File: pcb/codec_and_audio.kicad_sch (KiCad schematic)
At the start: 15 parts, among them IC3 PCM3060PWR, J3 AudioJack3_Dual_Switch, U1 ${SIM.PARAMS}

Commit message: progress on shcematics
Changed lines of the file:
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@@
     )
   )
-  (hierarchical_label "ENC_LRCK" (shape bidirectional) (at 125.095 97.79 180) (fields_autoplaced)
+  (hierarchical_label "ENC_LRCK" (shape input) (at 125.095 97.79 180) (fields_autoplaced)
     (effects (font (size 1.27 1.27)) (justify right))
   )
@@
     (effects (font (size 1.27 1.27)) (justify right))
   )
-  (hierarchical_label "DEC_LRCK" (shape bidirectional) (at 128.905 130.175 180) (fields_autoplaced)
+  (hierarchical_label "DEC_LRCK" (shape input) (at 128.905 130.175 180) (fields_autoplaced)
     (effects (font (size 1.27 1.27)) (justify right))
   )
@@
     (effects (font (size 1.27 1.27)) (justify right))
   )
-  (hierarchical_label "ENC_BCK" (shape bidirectional) (at 125.095 99.695 180) (fields_autoplaced)
+  (hierarchical_label "ENC_BCK" (shape input) (at 125.095 99.695 180) (fields_autoplaced)
     (effects (font (size 1.27 1.27)) (justify right))
   )
@@
     (effects (font (size 1.27 1.27)) (justify right))
   )
-  (hierarchical_label "DEC_BCK" (shape bidirectional) (at 128.905 128.27 180) (fields_autoplaced)
+  (hierarchical_label "DEC_BCK" (shape input) (at 128.905 128.27 180) (fields_autoplaced)
     (effects (font (size 1.27 1.27)) (justify right))
   )

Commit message: update
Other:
- moved on the sheet: C17, C18, J3A, R1, R2, U1

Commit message: i forgot this
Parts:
- removed C18: 330pF, symbol Device:C
- removed J3: AudioJack3_Dual_Switch, symbol Connector_Audio:AudioJack3_Dual_Switch
- removed R1: R, symbol Device:R
- removed R2: 20k, symbol Device:R
- removed U1: ${SIM.PARAMS}, symbol Simulation_SPICE:OPAMP
- added J3, J4: XLR3_AudioJack2_Combo_Ground, symbol Connector_Audio:XLR3_AudioJack2_Combo_Ground
- C17: value 10uF -> 4u7
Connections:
- net GND: now also J3.1, J3.G, J4.1, J4.G
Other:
- note added: "cold"
- note added: "hot"
- note removed: "high pass filter"
- note removed: "low pass filter"
- note removed: "sleeve is connected to VCOM"
- moved on the sheet: C10, C11, C12, C13, C14, C15, C16, C17, C9, IC3

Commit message: aaaaaa
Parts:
- removed C10, C11: 4.7uF, symbol Device:C_Polarized
- removed C12, C16, C9: 10uF, symbol Device:C_Polarized
- removed IC3: PCM3060PWR, SOP65P640X120-28N, symbol SamacSys_Parts:PCM3060PWR
- removed J4: XLR3_AudioJack2_Combo_Ground, symbol Connector_Audio:XLR3_AudioJack2_Combo_Ground
- added C10, C11, C18: 100nF, symbol Device:C
- added C12, C25, C9: 1uF, symbol Device:C
- added C16: 47uF, symbol Device:C
- added C33: 10uF, symbol Device:C_Polarized
- added C35: 1uF, symbol Device:C_Polarized
- added J4: AudioJack2, symbol Connector_Audio:AudioJack2
- added J5: XLR3_Ground, symbol Connector_Audio:XLR3_Ground
- added R2, R6: 10k, symbol Device:R
- added U1: CS4272, Package_SO:TSSOP-28_4.4x9.7mm_P0.65mm, symbol Audio:CS4272
- C13: value 100nF -> 1uF
- C17: value 4u7 -> 10uF
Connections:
- net VCC is gone; now on net VCOM: C13.1
- net GND: now also C10.1, C11.1, C12.2, C16.1, C18.2, C25.2, C35.2, C9.1, J5.1, J5.G, U1.20 (VA), U1.21 (AGND), U1.8 (DGND)
- net VCOM: now also C11.2, C35.1, R2.2, R6.1, U1.15 (VCOM); no longer C15.2
- net at C17.1: now also R2.1
- net at C17.2: now also J5.2
- net VDD renamed 3V3
- net 3V3: now also C10.2, C12.1, C9.2, U1.10 (VL), U1.9 (VD)
- new net: C15.2, C16.2, U1.22 (FILT+)
- new net: C33.1, R6.2
- new net: C33.2, J5.3
- new net 5V0: C18.1, C25.1
- new net CS_CCLK: U1.11 (SCL/CCLK(M0))
- new net CS_CDIN: U1.12 (SDA/CDIN(M1))
- new net CS_CS: U1.13 (AD0/~{CS}(I2S/~{LJ}))
- new net CS_LRCK: U1.4 (LRCK)
- new net CS_MCLK: U1.3 (MCLK)
- new net CS_RST: U1.14 (~{RST})
- new net CS_SCLK: U1.5 (SCLK)
- new net CS_SDIN: U1.7 (SDIN)
- new net CS_SDOUT: U1.6 (SDOUT(M/~{S}))
- no-connect marks 0 -> 4
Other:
- note added: "Input: from figure 12 of datasheet Output: from figure 14 of datasheet NOTE: the references have to be improved to support single ended signals"
- note added: "SCLK=64xFS LRCK=FS"
- note added: "input buffers"
- note added: "the datasheet says to avoid general purpose ceramics for high voltages to not worsen the linearity of the signal"
- note removed: "3v3 from power supply"
- note removed: "5v from power supply"
- note removed: "DGND, AGND1, AGND2, SGND all connected together"
- note removed: "Vcom is my A ref GND basically"
- note removed: "big circuit example b"
- note removed: "filtering stuff i guess"
- note removed: "now it's in SPI mode"
- note removed: "vcom is vcc/2"
- moved on the sheet: C14, C17, J3A

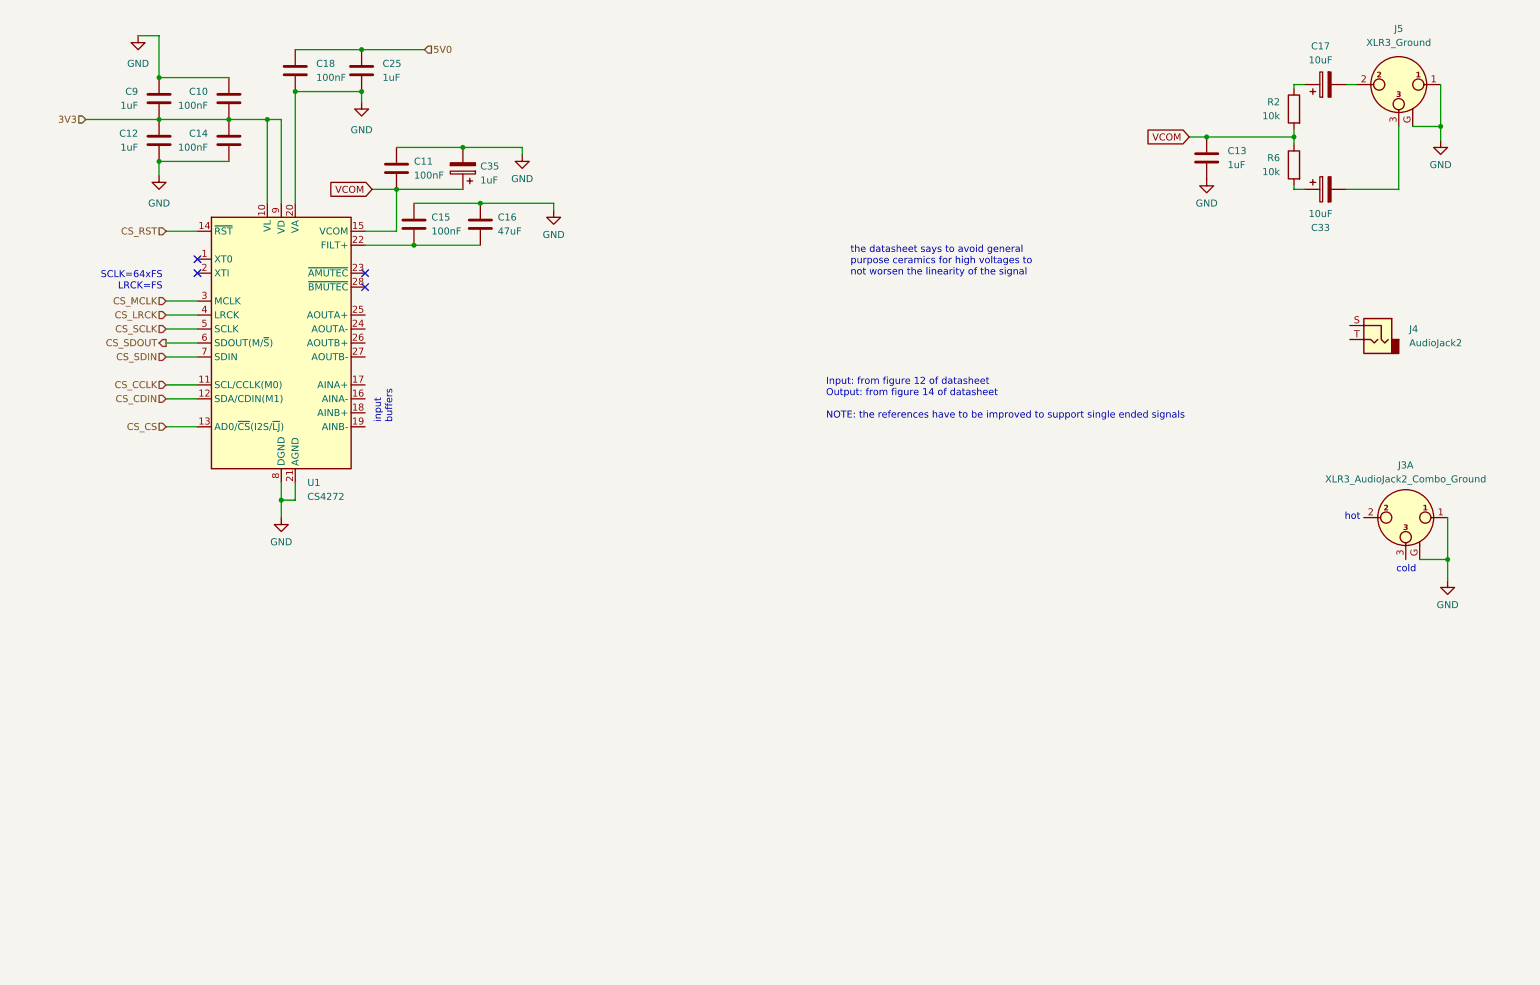
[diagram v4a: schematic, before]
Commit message: some more pages for the schematic
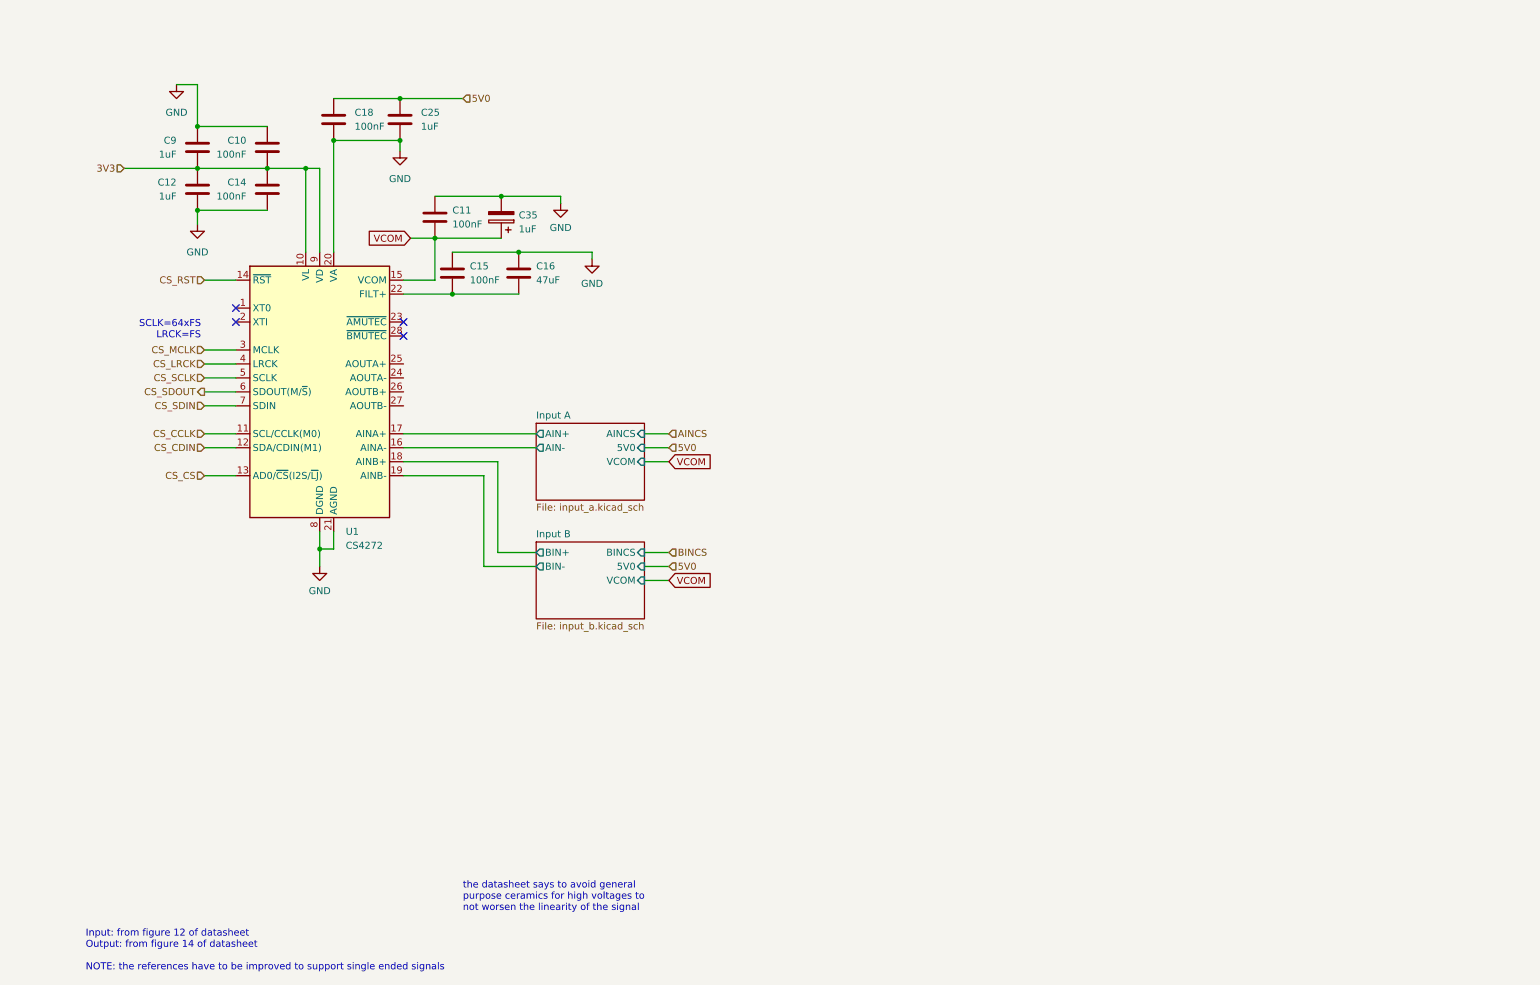
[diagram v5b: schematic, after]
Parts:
- removed C13: 1uF, symbol Device:C
- removed C17, C33: 10uF, symbol Device:C_Polarized
- removed J3: XLR3_AudioJack2_Combo_Ground, symbol Connector_Audio:XLR3_AudioJack2_Combo_Ground
- removed J4: AudioJack2, symbol Connector_Audio:AudioJack2
- removed J5: XLR3_Ground, symbol Connector_Audio:XLR3_Ground
- removed R2, R6: 10k, symbol Device:R
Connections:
- net Input A/AIN-: now reaches U1.16 (AINA-)
- net Input A/AIN+: now reaches U1.17 (AINA+)
- net Input B/BIN+: now reaches U1.18 (AINB+)
- net Input B/BIN-: now reaches U1.19 (AINB-)
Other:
- added sheet Input A (input_a.kicad_sch)
- added sheet Input B (input_b.kicad_sch)
- note removed: "cold"
- note removed: "hot"
- note removed: "input buffers"
- moved on the sheet: C10, C11, C12, C14, C15, C16, C18, C25, C35, C9, U1

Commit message: big progress!
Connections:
- net CS_CS is gone; now on net GND: U1.13 (AD0/~{CS}(I2S/~{LJ}))
- net Output A/AOUT-: now reaches U1.24 (AOUTA-)
- net Output A/AOUT+: now reaches U1.25 (AOUTA+)
- net Output B/BOUT+: now reaches U1.26 (AOUTB+)
- net Output B/BOUT-: now reaches U1.27 (AOUTB-)
- net CS_CCLK renamed CS_SCL
- net CS_CDIN renamed CS_SDA
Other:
- added sheet Output A (output_a.kicad_sch)
- added sheet Output B (output_b.kicad_sch)

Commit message: progress
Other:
- sheet Input A ports: added none; removed AINCS
- sheet Input B ports: added none; removed BINCS
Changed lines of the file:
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@@
-    (stroke (width 0) (type default))
-  )
-  (wire (pts (xy 125.73 128.27) (xy 130.175 128.27))
     (stroke (width 0) (type default))
   )
@@
   )
   (wire (pts (xy 45.72 76.835) (xy 51.435 76.835))
-    (stroke (width 0) (type default))
-  )
-  (wire (pts (xy 125.73 105.41) (xy 130.175 105.41))
     (stroke (width 0) (type default))
   )
@@
     (effects (font (size 1.27 1.27)) (justify right))
   )
-  (hierarchical_label "AINCS" (shape input) (at 130.175 105.41 0) (fields_autoplaced)
-    (effects (font (size 1.27 1.27)) (justify left))
-  )
   (hierarchical_label "CS_SDIN" (shape input) (at 45.72 86.995 180) (fields_autoplaced)
     (effects (font (size 1.27 1.27)) (justify right))
@@
   )
   (hierarchical_label "5V0" (shape input) (at 167.005 71.12 0) (fields_autoplaced)
-    (effects (font (size 1.27 1.27)) (justify left))
-  )
-  (hierarchical_label "BINCS" (shape input) (at 130.175 128.27 0) (fields_autoplaced)
     (effects (font (size 1.27 1.27)) (justify left))
   )
@@
       (effects (font (size 1.27 1.27)) (justify left))
     )
-    (pin "BINCS" input (at 125.73 128.27 0)
-      (effects (font (size 1.27 1.27)) (justify right))
-    )
     (pin "BIN+" output (at 106.045 128.27 180)
       (effects (font (size 1.27 1.27)) (justify left))
@@
       (effects (font (size 1.27 1.27)) (justify left))
     )
-    (pin "AINCS" input (at 125.73 105.41 0)
-      (effects (font (size 1.27 1.27)) (justify right))
-    )
     (pin "AIN-" output (at 106.045 107.95 180)

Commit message: making up my mind on the heaphones
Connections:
- net 3V3 renamed +3V3
- net 5V0 renamed +5V
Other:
- added sheet Output HP (output_hp.kicad_sch)
- sheet Input A ports: added none; removed 5V0
- sheet Input B ports: added none; removed 5V0
- sheet Output A ports: added AOUT_HP; removed 5V0
- sheet Output B ports: added BOUT_HP; removed 5V0
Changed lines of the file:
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@@
-    (stroke (width 0) (type default))
-  )
-  (wire (pts (xy 162.56 71.12) (xy 167.005 71.12))
     (stroke (width 0) (type default))
   )
@@
     (stroke (width 0) (type default))
   )
-  (wire (pts (xy 125.73 130.81) (xy 130.175 130.81))
-    (stroke (width 0) (type default))
-  )
   (wire (pts (xy 66.675 109.855) (xy 66.675 113.03))
     (stroke (width 0) (type default))
@@
     (stroke (width 0) (type default))
   )
-  (wire (pts (xy 162.56 93.98) (xy 167.005 93.98))
-    (stroke (width 0) (type default))
-  )
   (wire (pts (xy 116.205 60.325) (xy 116.205 59.055))
     (stroke (width 0) (type default))
@@
   )
   (wire (pts (xy 81.915 81.915) (xy 127 81.915))
-    (stroke (width 0) (type default))
-  )
-  (wire (pts (xy 125.73 107.95) (xy 130.175 107.95))
     (stroke (width 0) (type default))
   )
@@
   )
   (text "the datasheet says to avoid general\npurpose ceramics for high voltages to\nnot worsen the linearity of the signal"
-    (at 92.71 179.07 0)
+    (at 77.47 182.88 0)
     (effects (font (size 1.27 1.27)) (justify left bottom))
   )
@@
     (effects (font (size 1.27 1.27)) (justify right))
   )
-  (hierarchical_label "5V0" (shape input) (at 130.175 130.81 0) (fields_autoplaced)
-    (effects (font (size 1.27 1.27)) (justify left))
-  )
-  (hierarchical_label "5V0" (shape input) (at 167.005 71.12 0) (fields_autoplaced)
-    (effects (font (size 1.27 1.27)) (justify left))
-  )
-  (hierarchical_label "5V0" (shape input) (at 130.175 107.95 0) (fields_autoplaced)
-    (effects (font (size 1.27 1.27)) (justify left))
-  )
-  (hierarchical_label "5V0" (shape input) (at 167.005 93.98 0) (fields_autoplaced)
-    (effects (font (size 1.27 1.27)) (justify left))
-  )
   (hierarchical_label "CS_MCLK" (shape input) (at 45.72 76.835 180) (fields_autoplaced)
     (effects (font (size 1.27 1.27)) (justify right))
-  )
-  (hierarchical_label "3V3" (shape input) (at 31.115 43.815 180) (fields_autoplaced)
-    (effects (font (size 1.27 1.27)) (justify right))
-  )
-  (hierarchical_label "5V0" (shape input) (at 92.71 31.115 0) (fields_autoplaced)
-    (effects (font (size 1.27 1.27)) (justify left))
   )
   (hierarchical_label "CS_SDOUT" (shape output) (at 45.72 84.455 180) (fields_autoplaced)
@@
     )
   )
+  (symbol (lib_id "power:+5V") (at 92.71 31.115 0) (unit 1)
+    (in_bom yes) (on_board yes) (dnp no) (fields_autoplaced)
+    (property "Reference" "#PWR050" (at 92.71 34.925 0)
+      (effects (font (size 1.27 1.27)) hide)
+    )
+    (property "Value" "+5V" (at 92.71 26.67 0)
+      (effects (font (size 1.27 1.27)))
+    )
+    (property "Footprint" "" (at 92.71 31.115 0)
+      (effects (font (size 1.27 1.27)) hide)
+    )
+    (property "Datasheet" "" (at 92.71 31.115 0)
+      (effects (font (size 1.27 1.27)) hide)
+    )
+    (pin "1")
+    (instances
+      (project "bt_pcb"
+        (path "/eb787481-08cd-41a4-a128-173fa6227c32/4ada0139-8712-47ce-9d4c-ab8fef312f7b"
+          (reference "#PWR050") (unit 1)
+        )
+      )
+    )
+  )
   (symbol (lib_id "Device:C") (at 44.45 40.005 0) (mirror y) (unit 1)
     (in_bom yes) (on_board yes) (dnp no)
@@
         (path "/eb787481-08cd-41a4-a128-173fa6227c32/4ada0139-8712-47ce-9d4c-ab8fef312f7b"
           (reference "C9") (unit 1)
+        )
+      )
+    )
+  )
+  (symbol (lib_id "power:+3V3") (at 31.115 43.815 0) (unit 1)
+    (in_bom yes) (on_board yes) (dnp no) (fields_autoplaced)
+    (property "Reference" "#PWR048" (at 31.115 47.625 0)
+      (effects (font (size 1.27 1.27)) hide)
+    )
+    (property "Value" "+3V3" (at 31.115 38.735 0)
+      (effects (font (size 1.27 1.27)))
+    )
+    (property "Footprint" "" (at 31.115 43.815 0)
+      (effects (font (size 1.27 1.27)) hide)
+    )
+    (property "Datasheet" "" (at 31.115 43.815 0)
+      (effects (font (size 1.27 1.27)) hide)
+    )
+    (pin "1")
+    (instances
+      (project "bt_pcb"
+        (path "/eb787481-08cd-41a4-a128-173fa6227c32/4ada0139-8712-47ce-9d4c-ab8fef312f7b"
+          (reference "#PWR048") (unit 1)
         )
       )
@@
       (effects (font (size 1.27 1.27)) (justify left))
     )
-    (pin "5V0" input (at 125.73 130.81 0)
-      (effects (font (size 1.27 1.27)) (justify right))
-    )
     (pin "VCOM" input (at 125.73 133.35 0)
       (effects (font (size 1.27 1.27)) (justify right))
@@
       (effects (font (size 1.27 1.27)) (justify left))
     )
-    (pin "5V0" input (at 162.56 71.12 0)
+    (pin "AOUT_HP" output (at 162.56 81.28 0)
       (effects (font (size 1.27 1.27)) (justify right))
     )
@@
       (project "bt_pcb"
         (path "/eb787481-08cd-41a4-a128-173fa6227c32/4ada0139-8712-47ce-9d4c-ab8fef312f7b" (page "6"))
+      )
+    )
+  )
+  (sheet (at 179.07 118.745) (size 19.05 8.255) (fields_autoplaced)
+    (stroke (width 0.1524) (type solid))
+    (fill (color 0 0 0 0.0000))
+    (property "Sheetname" "Output HP" (at 179.07 118.0334 0)
+      (effects (font (size 1.27 1.27)) (justify left bottom))
+    )
+    (property "Sheetfile" "output_hp.kicad_sch" (at 179.07 127.5846 0)
+      (effects (font (size 1.27 1.27)) (justify left top))
+    )
+    (property "Campo2" "" (at 179.07 118.745 0)
+      (effects (font (size 1.27 1.27)) hide)
+    )
+    (instances
+      (project "bt_pcb"
+        (path "/eb787481-08cd-41a4-a128-173fa6227c32/4ada0139-8712-47ce-9d4c-ab8fef312f7b" (page "9"))
       )
     )
@@
       (effects (font (size 1.27 1.27)) (justify left))
     )
-    (pin "5V0" input (at 162.56 93.98 0)
+    (pin "VCOM" input (at 162.56 96.52 0)
       (effects (font (size 1.27 1.27)) (justify right))
     )
-    (pin "VCOM" input (at 162.56 96.52 0)
+    (pin "BOUT_HP" output (at 162.56 104.14 0)
       (effects (font (size 1.27 1.27)) (justify right))
     )
@@
       (effects (font (size 1.27 1.27)) (justify right))
     )
-    (pin "5V0" input (at 125.73 107.95 0)
-      (effects (font (size 1.27 1.27)) (justify right))
-    )
